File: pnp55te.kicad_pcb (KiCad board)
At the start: 2 copper layers, 154 x 109 mm, 67 parts, among them U1 TPIC8101, U3 molex_48pin_MRE, X1 55pin_january_5.1

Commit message: DRAFT
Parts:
- added J1: Conn_01x01, Connector_PinSocket_2.00mm:PinSocket_1x01_P2.00mm_Vertical, F.Cu at (170.3, 62.7)
- added J2: Conn_01x01, Connector_PinSocket_2.00mm:PinSocket_1x01_P2.00mm_Vertical, F.Cu at (170.3, 67.8)
- added J3: Conn_01x01, Connector_PinSocket_2.00mm:PinSocket_1x01_P2.00mm_Vertical, F.Cu at (151.1, 58.4)
- added J4: Conn_01x01, Connector_PinSocket_2.00mm:PinSocket_1x01_P2.00mm_Vertical, F.Cu at (151.1, 61.6)
- added J5: Conn_01x01, Connector_PinSocket_2.00mm:PinSocket_1x01_P2.00mm_Vertical, F.Cu at (163.8, 58.4)
- added J6: Conn_01x01, Connector_PinSocket_2.00mm:PinSocket_1x01_P2.00mm_Vertical, F.Cu at (164.5, 72.4)
- added J7: Conn_01x01, Connector_PinSocket_2.00mm:PinSocket_1x01_P2.00mm_Vertical, F.Cu at (101.6, 139.7)
- added J8: Conn_01x01, Connector_PinSocket_2.00mm:PinSocket_1x01_P2.00mm_Vertical, F.Cu at (103.5, 135.3)
- added U2: VNLD5090, Package_SO:SO-8_3.9x4.9mm_P1.27mm, F.Cu at (151.1, 66.0)
- added U4: VNLD5090, Package_SO:SO-8_3.9x4.9mm_P1.27mm, F.Cu at (164.0, 65.9)
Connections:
- net /PB9 renamed /J806_PB9
- U1 pad 10: (no net) -> Net-(U1-Pad10)
- U1 pad 14: (no net) -> Net-(U1-Pad14)
- U1 pad 9: (no net) -> Net-(U1-Pad9)
- U3 pad 15: (no net) -> /USBD-
- U3 pad 16: (no net) -> /USBD+
- U3 pad 4: (no net) -> Net-(U3-Pad4)
- U3 pad 44: (no net) -> /5V_SENS1
- U3 pad 8: (no net) -> Net-(U3-Pad8)
- U3 pad J51: (no net) -> Net-(U3-PadJ51)
- U3 pad J52: (no net) -> Net-(U3-PadJ52)
- U3 pad J53: (no net) -> Net-(U3-PadJ53)
- U3 pad J54: (no net) -> Net-(U3-PadJ54)
- U3 pad J802: (no net) -> Net-(J7-Pad1)
- U3 pad J803: (no net) -> /J803_PB8
- U3 pad J804: (no net) -> /MRE_3V3
- U3 pad M11: (no net) -> Net-(U3-PadM11)
- U3 pad M12: (no net) -> Net-(U3-PadM12)
- U3 pad M13: (no net) -> Net-(U3-PadM13)
- U3 pad M21: (no net) -> Net-(U3-PadM21)
- U3 pad M22: (no net) -> Net-(U3-PadM22)
- U3 pad M23: (no net) -> Net-(U3-PadM23)
- U3 pad M3: (no net) -> Net-(U3-PadM3)
- U3 pad M4: (no net) -> Net-(U3-PadM4)
- U3 pad M51: (no net) -> Net-(U3-PadM51)
- U3 pad M52: (no net) -> Net-(U3-PadM52)
- U3 pad M53: (no net) -> Net-(U3-PadM53)
- U3 pad M61: (no net) -> Net-(U3-PadM61)
- U3 pad M62: (no net) -> Net-(U3-PadM62)
- U3 pad M63: (no net) -> Net-(U3-PadM63)
- U3 pad M71: (no net) -> Net-(U3-PadM71)
- U3 pad M72: (no net) -> Net-(U3-PadM72)
- U3 pad M73: (no net) -> Net-(U3-PadM73)
- W32 pad 2: Net-(W32-Pad2) -> /EXTRA_LOW_SIDE_DRIVE1
- W47 pad 2: Net-(W47-Pad2) -> /EXTRA_LOW_SIDE_DRIVE2
- X1 pad 9: (no net) -> /SPEED_SENS
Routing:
- net /J803_PB8: track 0.00 -> 99.5 mm, vias 0 -> 1
- net /J806_PB9: track 80.4 -> 177.0 mm, vias 0 -> 1
- net /PA15_SPI3CS: track 85.1 -> 173.9 mm, vias 0 -> 1
- net /PC12_SPI3MOSI: track 84.7 -> 171.0 mm, vias 0 -> 1
- net /EXTRA_LOW_SIDE_DRIVE2: track 0.00 -> 61.6 mm, vias 0 -> 1
- net /EXTRA_LOW_SIDE_DRIVE1: track 0.00 -> 40.1 mm, vias 0 -> 1
- net GND: track 342.4 -> 359.4 mm, vias 53 -> 405
- net Net-(J3-Pad1): track 0.00 -> 11.5 mm
- net /12_MAIN_RELAY: track 139.6 -> 149.9 mm, vias 0 -> 2
- net Net-(J5-Pad1): track 0.00 -> 8.91 mm
- net Net-(J7-Pad1): track 0.00 -> 6.92 mm
- net Net-(J6-Pad1): track 0.00 -> 6.48 mm
- net /MRE_3V3: track 0.00 -> 4.98 mm
- net Net-(J4-Pad1): track 0.00 -> 4.72 mm
- net /EXTRA_LOW_SIDE_DRIVE4: track 0.00 -> 4.30 mm
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
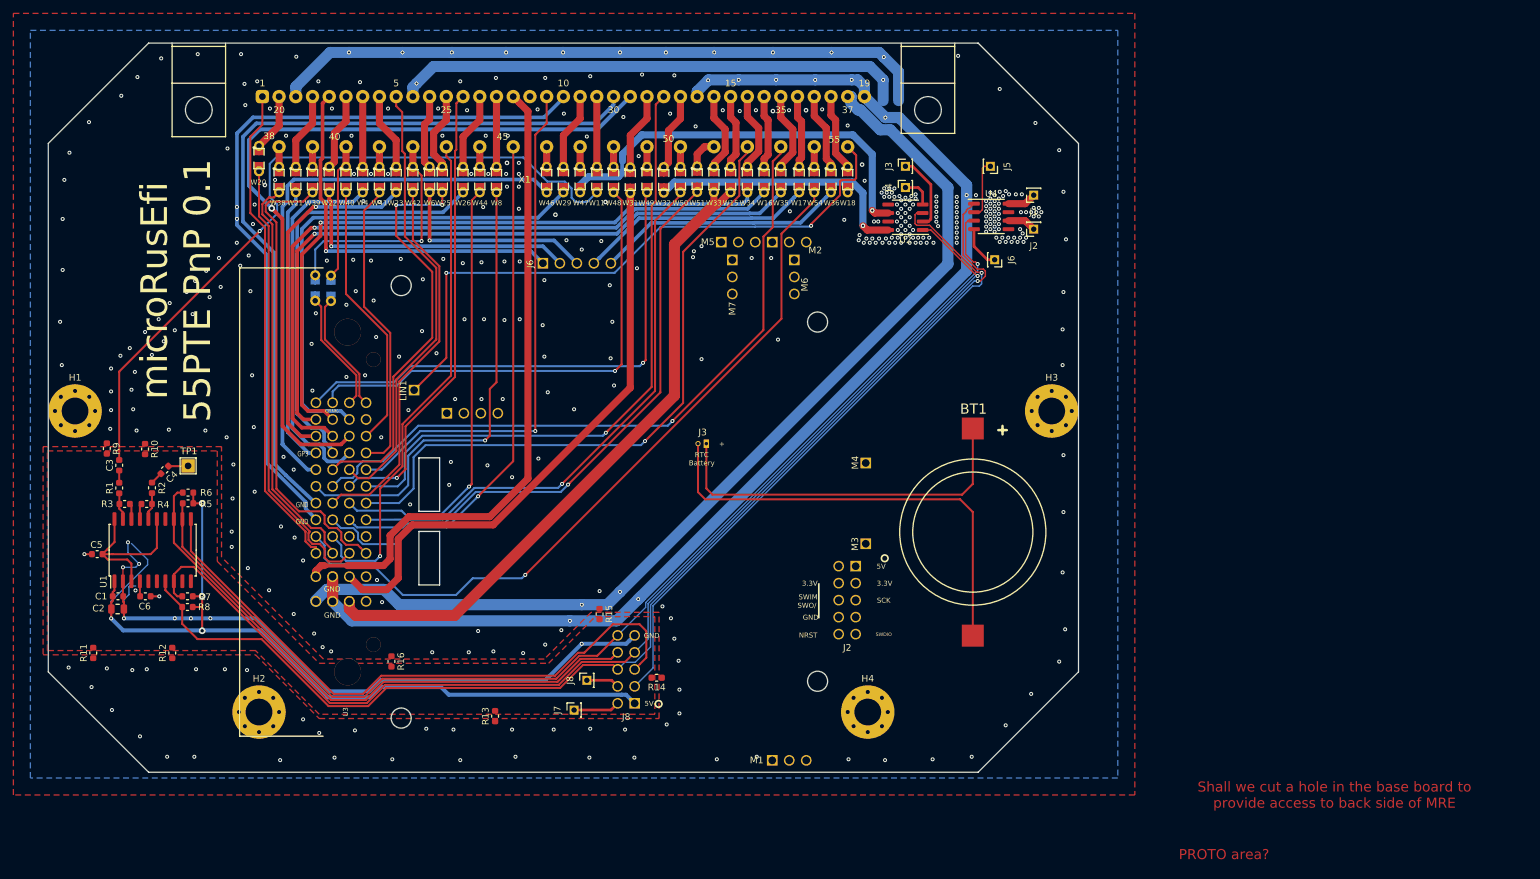
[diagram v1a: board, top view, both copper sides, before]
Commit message: Sorry, revert these changes
I do not want ONE-BIG-SINGLE ground plane. Sorry.
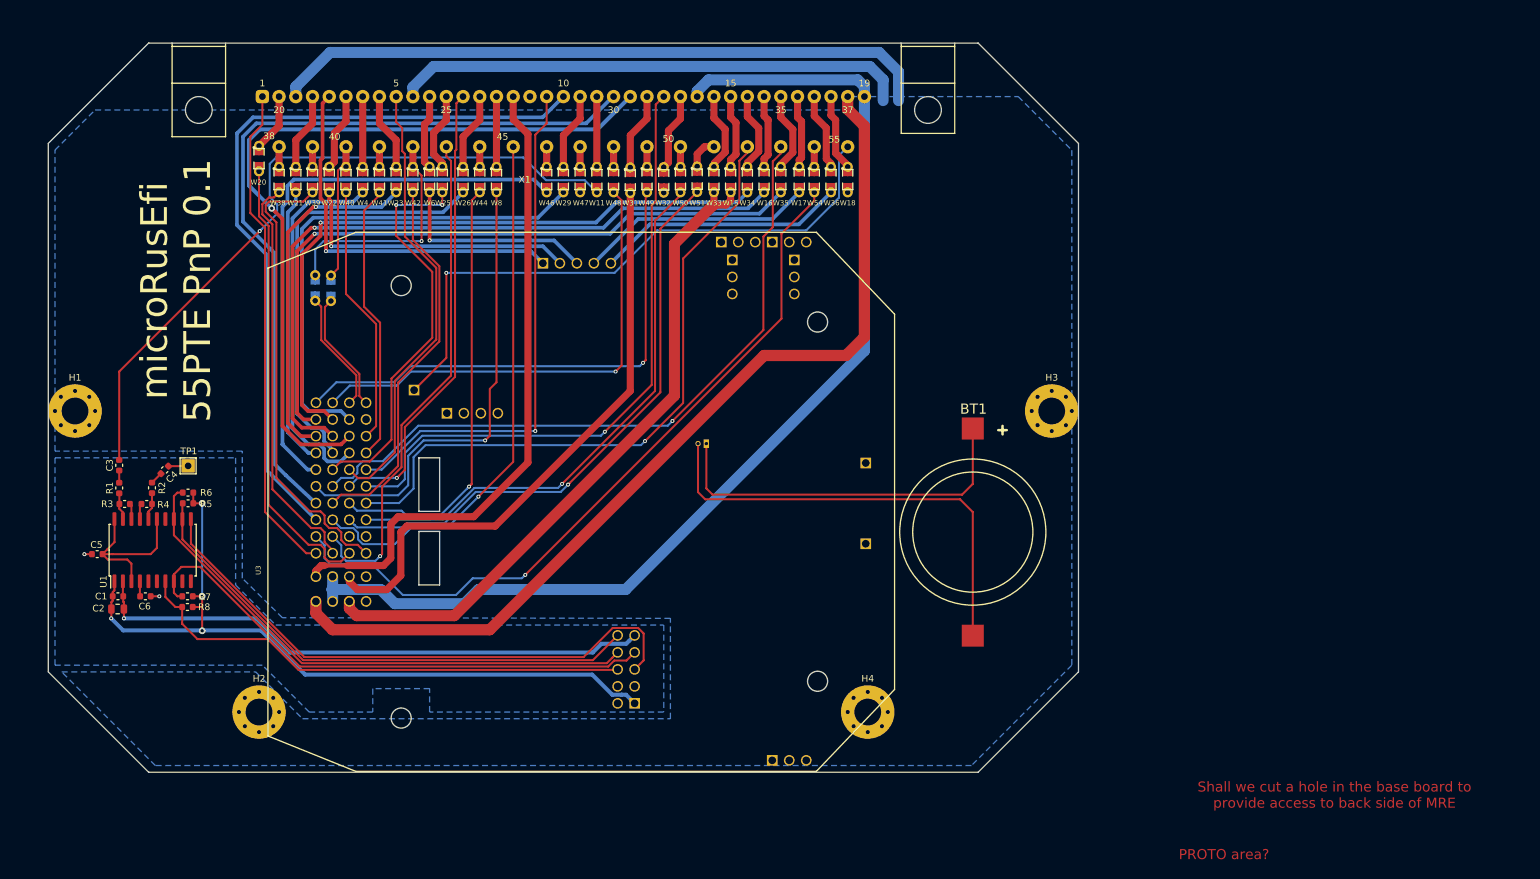
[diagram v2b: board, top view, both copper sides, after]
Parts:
- removed J1, J2, J3, J4, J5, J6, J7, J8: Conn_01x01, Connector_PinSocket_2.00mm:PinSocket_1x01_P2.00mm_Vertical
- removed R10, R11, R12, R13, R14, R15, R16, R9: DNP, Resistor_SMD:R_0603_1608Metric
- removed U2, U4: VNLD5090, Package_SO:SO-8_3.9x4.9mm_P1.27mm
- R1, R2, R3, R4: value 39K -> R
- R5, R6, R7: value DNP -> R
- R8: value 5K -> R
- U3: footprint rusEFI_Modules:Molex_48_MRE -> hw_55_te:Molex_48_MRE_clean
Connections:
- net /J806_PB9 renamed /PB9
- U1 pad 10: Net-(U1-Pad10) -> (no net)
- U1 pad 14: Net-(U1-Pad14) -> (no net)
- U1 pad 9: Net-(U1-Pad9) -> (no net)
- U3 pad 15: /USBD- -> (no net)
- U3 pad 16: /USBD+ -> (no net)
- U3 pad 4: Net-(U3-Pad4) -> (no net)
- U3 pad 44: /5V_SENS1 -> (no net)
- U3 pad 8: Net-(U3-Pad8) -> (no net)
- U3 pad J51: Net-(U3-PadJ51) -> (no net)
- U3 pad J52: Net-(U3-PadJ52) -> (no net)
- U3 pad J53: Net-(U3-PadJ53) -> (no net)
- U3 pad J54: Net-(U3-PadJ54) -> (no net)
- U3 pad J802: Net-(J7-Pad1) -> (no net)
- U3 pad J803: /J803_PB8 -> (no net)
- U3 pad J804: /MRE_3V3 -> (no net)
- U3 pad M11: Net-(U3-PadM11) -> (no net)
- U3 pad M12: Net-(U3-PadM12) -> (no net)
- U3 pad M13: Net-(U3-PadM13) -> (no net)
- U3 pad M21: Net-(U3-PadM21) -> (no net)
- U3 pad M22: Net-(U3-PadM22) -> (no net)
- U3 pad M23: Net-(U3-PadM23) -> (no net)
- U3 pad M3: Net-(U3-PadM3) -> (no net)
- U3 pad M4: Net-(U3-PadM4) -> (no net)
- U3 pad M51: Net-(U3-PadM51) -> (no net)
- U3 pad M52: Net-(U3-PadM52) -> (no net)
- U3 pad M53: Net-(U3-PadM53) -> (no net)
- U3 pad M61: Net-(U3-PadM61) -> (no net)
- U3 pad M62: Net-(U3-PadM62) -> (no net)
- U3 pad M63: Net-(U3-PadM63) -> (no net)
- U3 pad M71: Net-(U3-PadM71) -> (no net)
- U3 pad M72: Net-(U3-PadM72) -> (no net)
- U3 pad M73: Net-(U3-PadM73) -> (no net)
- W32 pad 2: /EXTRA_LOW_SIDE_DRIVE1 -> Net-(W32-Pad2)
- W47 pad 2: /EXTRA_LOW_SIDE_DRIVE2 -> Net-(W47-Pad2)
- X1 pad 9: /SPEED_SENS -> (no net)
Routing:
- net /PB9: track 177.0 -> 76.0 mm, vias 1 -> 0
- net /J803_PB8: track 99.5 -> 0.00 mm, vias 1 -> 0
- net /PA15_SPI3CS: track 173.9 -> 80.6 mm, vias 1 -> 0
- net /PC12_SPI3MOSI: track 171.0 -> 79.5 mm, vias 1 -> 0
- net /EXTRA_LOW_SIDE_DRIVE2: track 61.6 -> 0.00 mm, vias 1 -> 0
- net /EXTRA_LOW_SIDE_DRIVE1: track 40.1 -> 0.00 mm, vias 1 -> 0
- net /MRE_GND: track 107.1 -> 87.6 mm, vias 11 -> 3
- net GND: track 359.4 -> 342.4 mm, vias 405 -> 0
- net /MRE_5V: track 129.8 -> 114.1 mm
- net Net-(J3-Pad1): track 11.5 -> 0.00 mm
- net /12_MAIN_RELAY: track 149.9 -> 139.9 mm, vias 2 -> 0
- net Net-(J5-Pad1): track 8.91 -> 0.00 mm
- net Net-(J7-Pad1): track 6.92 -> 0.00 mm
- net Net-(J6-Pad1): track 6.48 -> 0.00 mm
- net /PC11_SPI3MISO: track 92.9 -> 86.4 mm
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- added copper zone on B.Cu, net /MRE_GND
- removed copper zone on F.Cu, net /MRE_GND
- removed copper zone on F.Cu, net GND

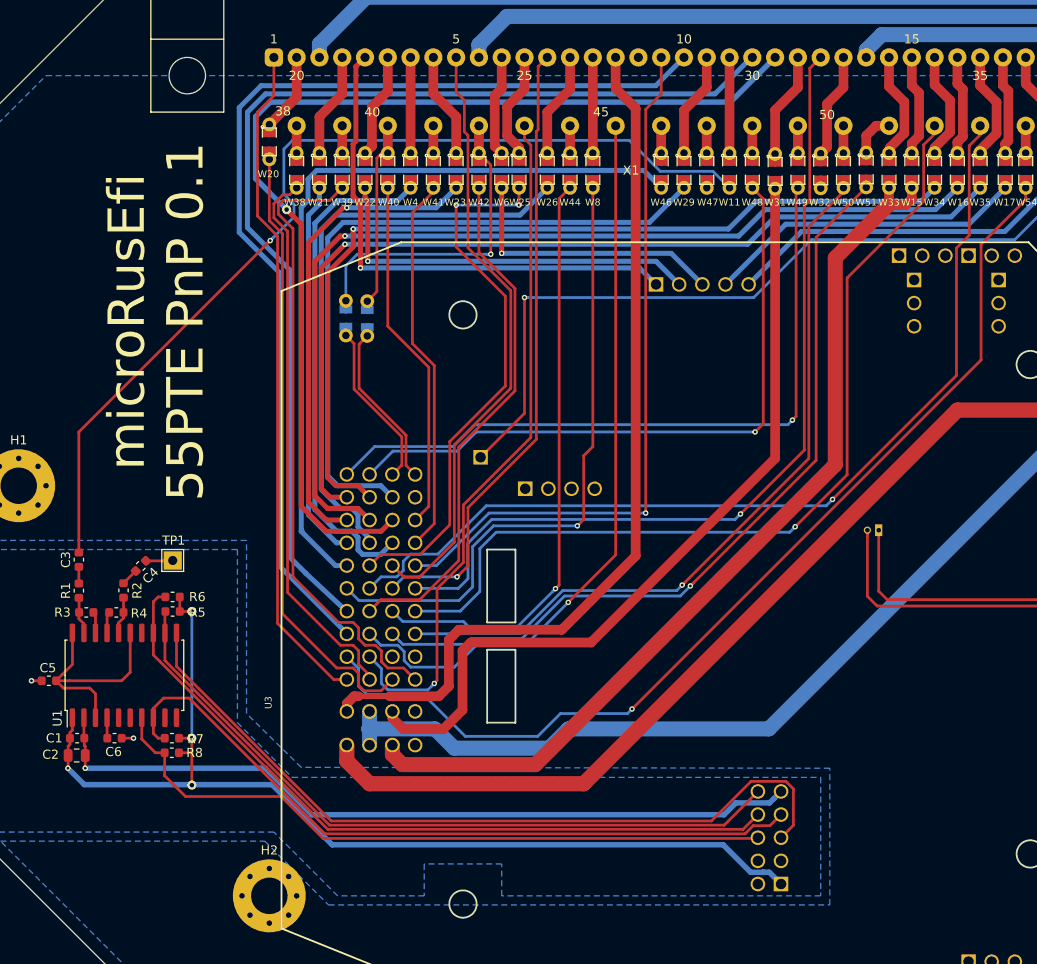
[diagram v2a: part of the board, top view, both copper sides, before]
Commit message: Oscilator for knock sensor, route knock sensor out to AIN, misc fixes
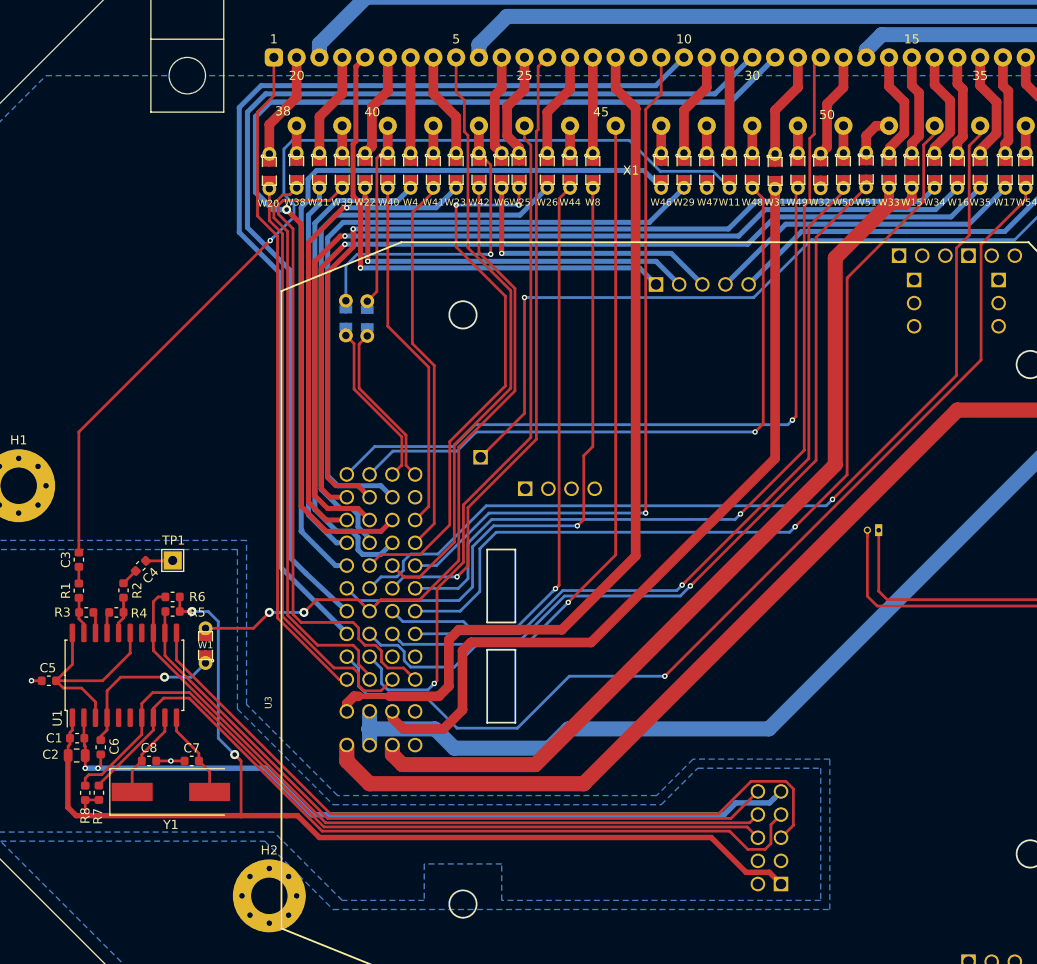
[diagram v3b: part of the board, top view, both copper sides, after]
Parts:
- added C7: 18pF, Capacitor_SMD:C_0603_1608Metric, F.Cu at (46.0, 125.2)
- added C8: 18pF, Capacitor_SMD:C_0603_1608Metric, F.Cu at (41.3, 125.2)
- added W1: n.a. TestPoint_2Pole, rusEFI_Modules:SM0805_jumper, F.Cu at (47.5, 112.5)
- added Y1: 8MHz, Crystal:Crystal_SMD_HC49-SD, F.Cu at (43.7, 128.6)
- moved R8 10.5 mm to (34.3, 128.7), turned to 270 degrees
- moved R7 10.0 mm to (35.8, 128.7), turned to 90 degrees
- moved W20 3.22 mm to (54.5, 60.5)
- moved C6 1.81 mm to (36.0, 123.7), turned to 270 degrees
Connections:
- U1 pad 10: (no net) -> Net-(C7-Pad1)
- U1 pad 9: (no net) -> Net-(C8-Pad1)
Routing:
- net /RESERVED_AIN1: track 57.2 -> 77.0 mm, vias 0 -> 2
- net Net-(C6-Pad1): track 2.26 -> 17.8 mm, vias 0 -> 1
- net /PB9: track 76.0 -> 87.1 mm
- net Net-(C7-Pad1): track 0.00 -> 9.66 mm
- net Net-(C8-Pad1): track 0.00 -> 9.64 mm
- net /MRE_5V: track 114.1 -> 123.6 mm, vias 4 -> 2
- net /PA15_SPI3CS: track 80.6 -> 90.0 mm
- net /MRE_GND: track 87.6 -> 91.0 mm, vias 3 -> 4
- net /COIL2: track 67.3 -> 64.3 mm
- net Net-(W20-Pad1): track 8.61 -> 11.6 mm
- net /HI4_UNUSED: track 68.7 -> 71.1 mm
- net Net-(C5-Pad1): track 26.4 -> 24.7 mm
- net /HI2_UNUSED: track 60.6 -> 62.1 mm
- net /PC11_SPI3MISO: track 86.4 -> 85.4 mm
- net /PC12_SPI3MOSI: track 79.5 -> 78.6 mm
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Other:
- board text added: "microRusEfi 55PTE PnP D0G V0.1"
- board text removed: "microRusEfi 55PTE PnP 0.1"
